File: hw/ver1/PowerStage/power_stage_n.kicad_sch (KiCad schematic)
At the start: 17 parts, among them Q1 MCAC80N10Y, Q2 MCAC80N10Y, U1 HIP2210

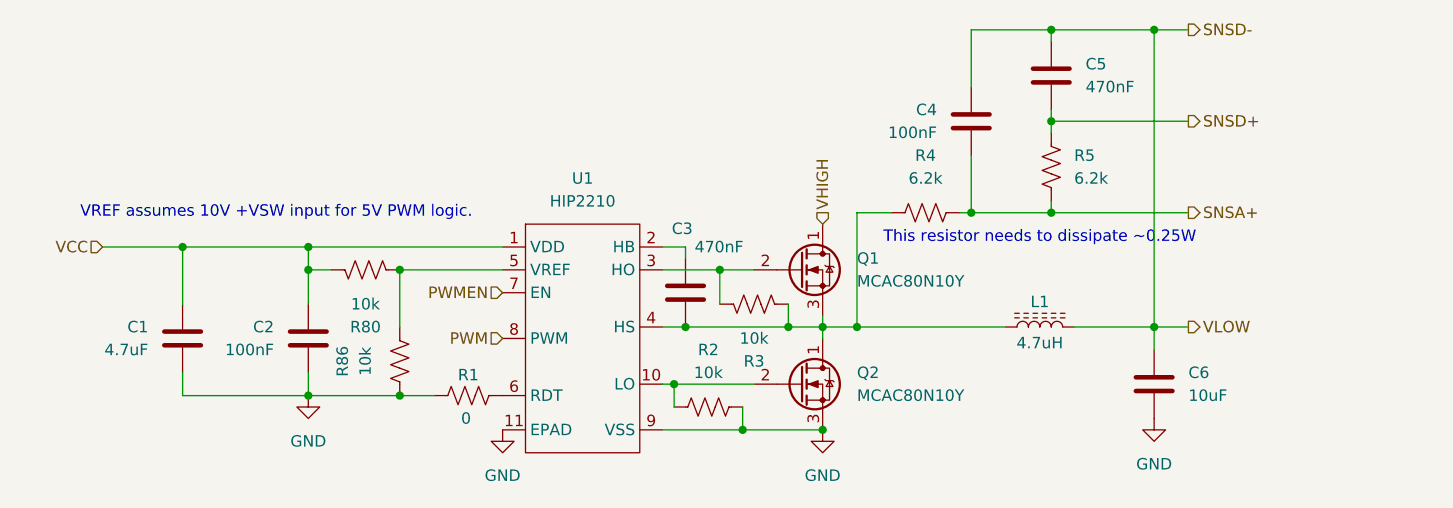
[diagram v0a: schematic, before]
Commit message: More power plane work. Double mosfets.
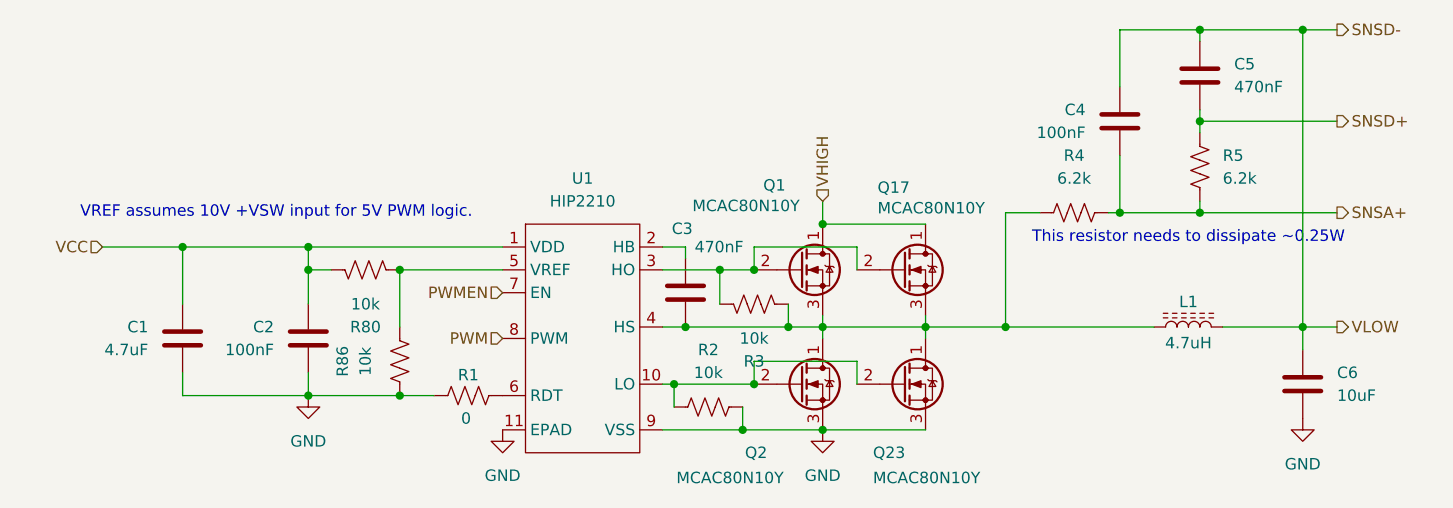
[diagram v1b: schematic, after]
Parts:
- added Q17, Q23: MCAC80N10Y, Mosfets:TRANS_BSC076N06NS3-G, symbol ProjectMosfets:MCAC80N10Y
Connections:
- net GND: now also Q23.3 (S)
- net VHIGH: now also Q17.1 (D)
- net at Q2.2 (G), R2.2, U1.10 (LO): now also Q23.2 (G)
- net at C3.2, L1.1, Q1.3 (S)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: now also Q17.3 (S), Q23.1 (D)
- net at Q1.2 (G), R3.2, U1.3 (HO): now also Q17.2 (G)
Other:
- moved on the sheet: C4, C5, C6, L1, R4, R5

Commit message: Sync lunch work
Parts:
- Q1, Q17, Q2, Q23: DigiKey (none) -> 353-MCAC80N10Y-TPCT-ND
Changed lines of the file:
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@@
+			)
+		)
+		(property "DigiKey" "353-MCAC80N10Y-TPCT-ND"
+			(at 177.8 83.82 0)
+			(effects
+				(font
+					(size 1.27 1.27)
+				)
+				(hide yes)
 			)
 		)
@@
 			)
 		)
-		(property "Datasheet" "https://www.bourns.com/docs/Product-Datasheets/PQ2614.pdf"
+		(property "Datasheet" "~"
 			(at 209.55 77.47 0)
 			(effects
@@
 		)
 		(property "LCSC" "N/A"
+			(at 177.8 71.12 0)
+			(effects
+				(font
+					(size 1.27 1.27)
+				)
+				(hide yes)
+			)
+		)
+		(property "DigiKey" "353-MCAC80N10Y-TPCT-ND"
 			(at 177.8 71.12 0)
 			(effects
@@
 			)
 		)
+		(property "DigiKey" "353-MCAC80N10Y-TPCT-ND"
+			(at 166.37 71.12 0)
+			(effects
+				(font
+					(size 1.27 1.27)
+				)
+				(hide yes)
+			)
+		)
 		(pin "1"
 		)
@@
 			(at 166.37 83.82 0)
 			(effects
+				(font
+					(size 1.27 1.27)
+				)
+				(hide yes)
+			)
+		)
+		(property "DigiKey" "353-MCAC80N10Y-TPCT-ND"
+			(at 166.37 83.82 0)
+			(effects

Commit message: Sync lunch work
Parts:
- C6: value 10uF -> 10uF-75V; LCSC (none) -> N/A
- R4: value 6.2k -> 6.2k-0.25w
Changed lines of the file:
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@@
 			)
 		)
-		(property "Value" "10uF"
+		(property "Value" "10uF-75V"
 			(at 226.06 85.0899 0)
 			(effects
@@
 		)
 		(property "Digikey" "445-CGA6P1X7R1N106M250ACCT-ND"
+			(at 222.25 83.82 0)
+			(effects
+				(font
+					(size 1.27 1.27)
+				)
+				(hide yes)
+			)
+		)
+		(property "LCSC" "N/A"
 			(at 222.25 83.82 0)
 			(effects
@@
 			)
 		)
-		(property "Value" "6.2k"
+		(property "Value" "6.2k-0.25w"
 			(at 196.85 60.96 90)
 			(effects
